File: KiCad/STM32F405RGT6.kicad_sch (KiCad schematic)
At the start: 1 part, among them U1 STM32F405RGTx

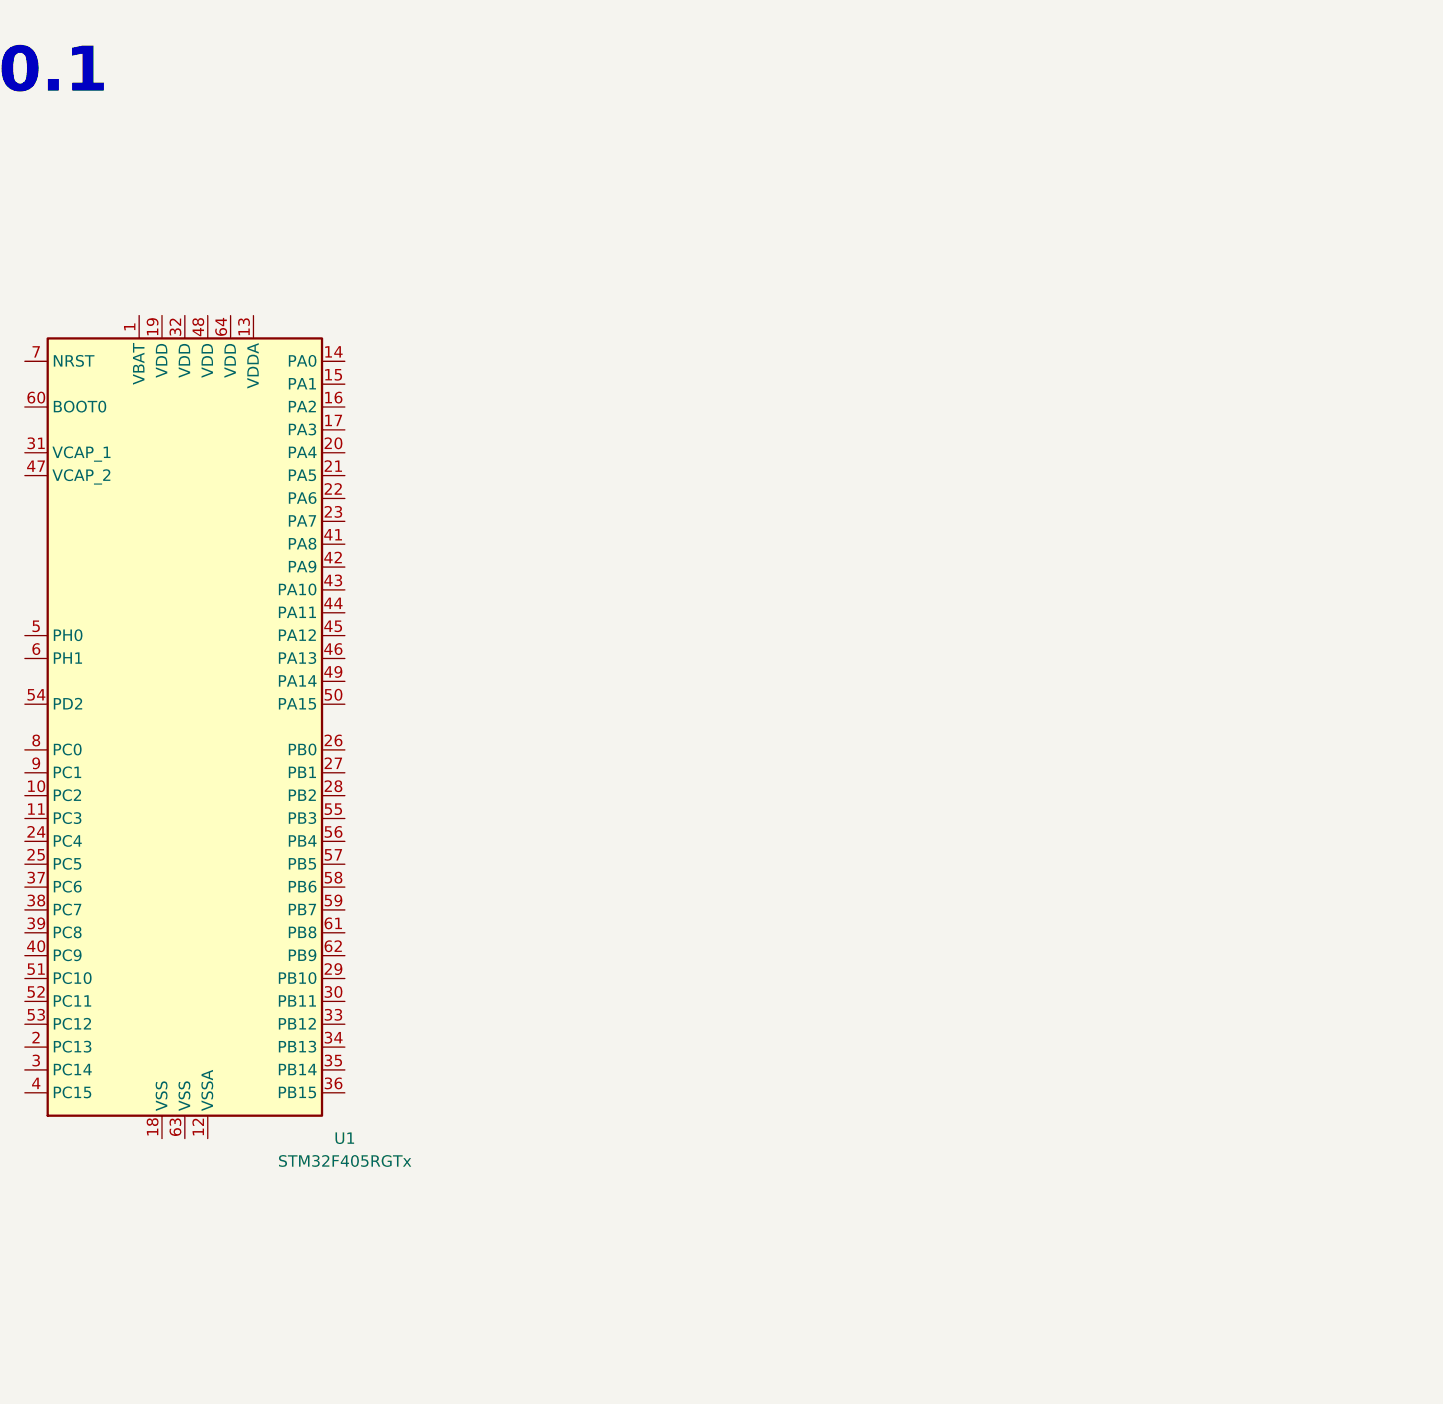
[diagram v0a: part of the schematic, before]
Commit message: Added prototype components to schematic
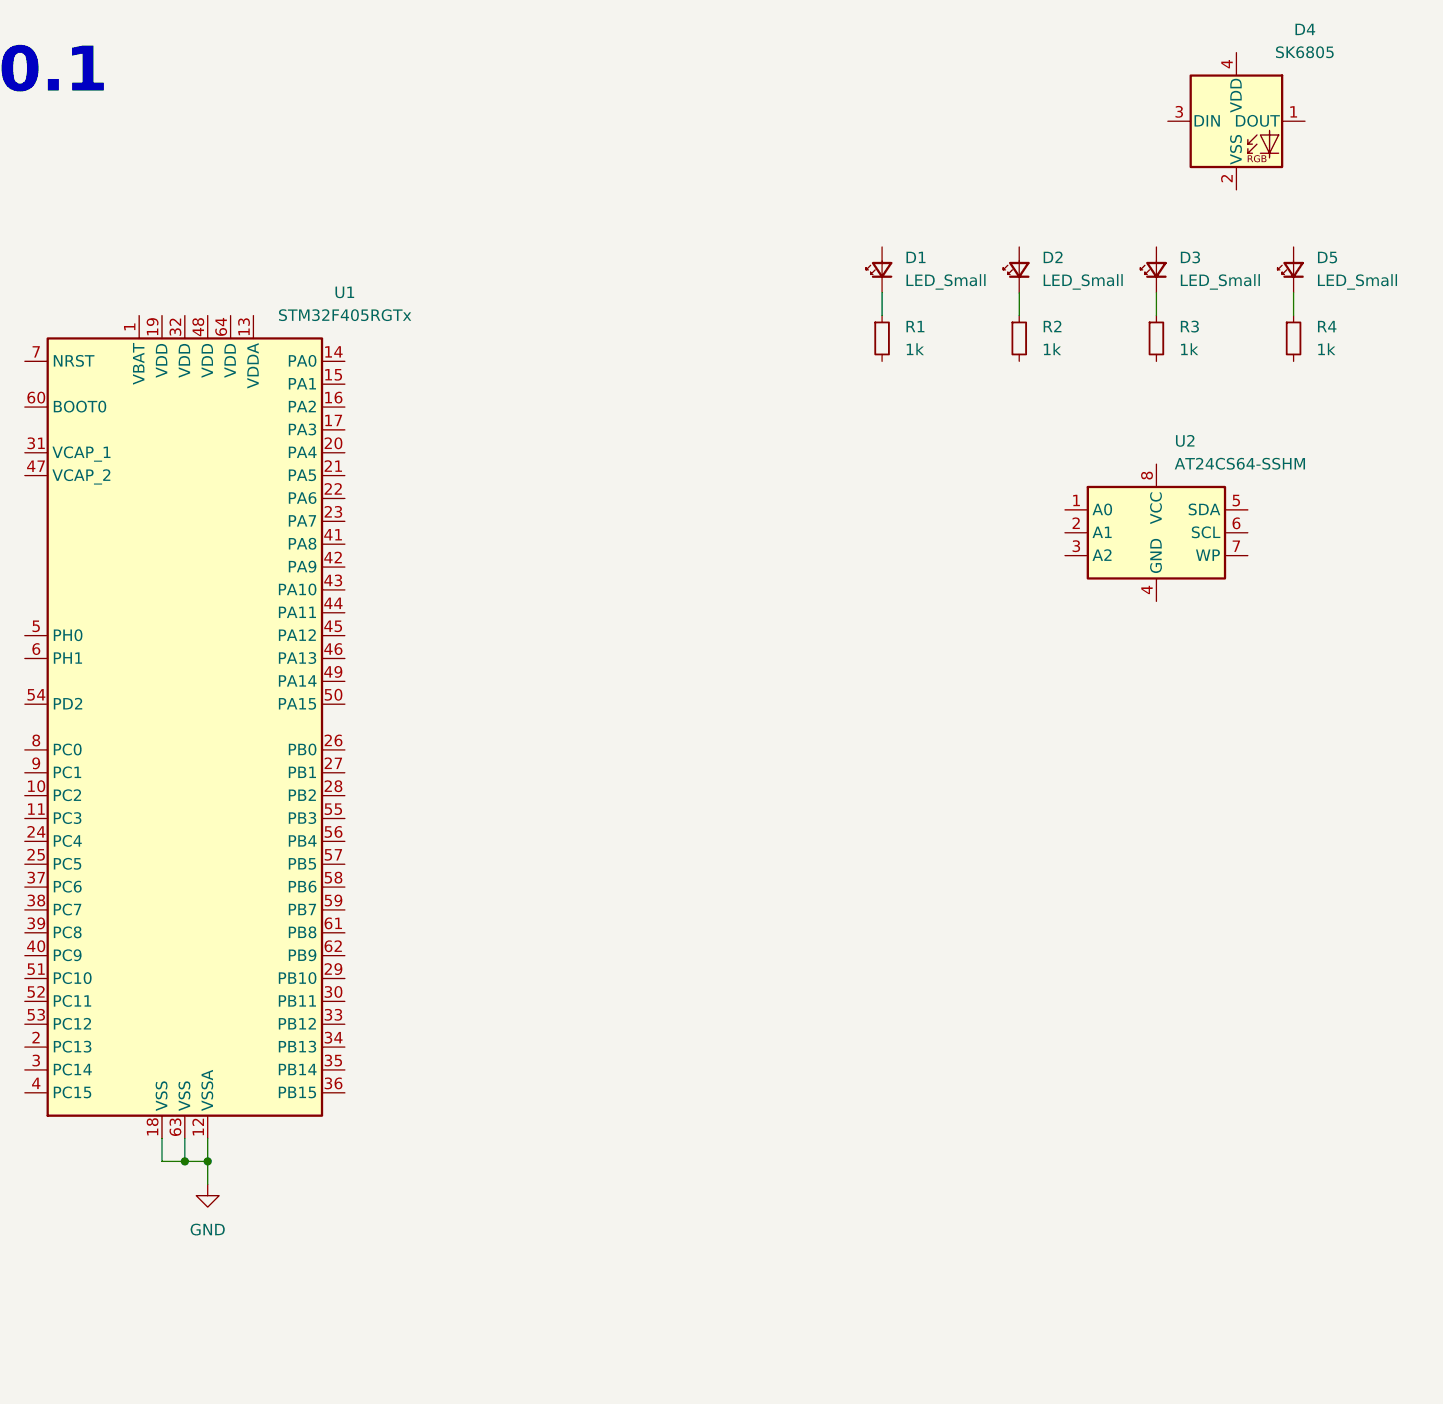
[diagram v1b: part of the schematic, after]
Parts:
- added D1, D2, D3, D5: LED_Small, LED_SMD:LED_0603_1608Metric, symbol Device:LED_Small
- added D4: SK6805, LED_SMD:LED_SK6805_PLCC4_2.4x2.7mm_P1.3mm, symbol LED:SK6805
- added R1, R2, R3, R4: 1k, Resistor_SMD:R_0603_1608Metric, symbol Device:R_Small
- added U2: AT24CS64-SSHM, Package_SO:SOIC-8_3.9x4.9mm_P1.27mm, symbol Memory_EEPROM:AT24CS64-SSHM
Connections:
- net GND: now reaches U1.12 (VSSA)
- net GND: now also U1.18 (VSS), U1.63 (VSS)
- new net: D3.1 (K), R3.1
- new net: D2.1 (K), R2.1
- new net: D1.1 (K), R1.1
- new net: D5.1 (K), R4.1

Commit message: Added Components to the Schematic and PCB
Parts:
- added C1, C11, C3, C5, C7, C8, C9: 100nF, Capacitor_SMD:C_0603_1608Metric, symbol Device:C_Small
- added C10: 1uF, Capacitor_SMD:C_0805_2012Metric, symbol Device:C_Small
- added C2: 10uF, Capacitor_SMD:C_0805_2012Metric, symbol Device:C_Small
- added C4, C6: 2.2uF, Capacitor_SMD:C_0805_2012Metric, symbol Device:C_Small
- added D6, D7: LED_Small, LED_SMD:LED_0603_1608Metric, symbol Device:LED_Small
- added FB1, FB2: FerriteBead_Small, Inductor_SMD:L_0805_2012Metric, symbol Device:FerriteBead_Small
- added J1, J2: USB_C_Receptacle_USB2.0, Connector_USB:USB_C_Receptacle_HRO_TYPE-C-31-M-12, symbol Connector:USB_C_Receptacle_USB2.0
- added R5, R6: 1k, Resistor_SMD:R_0603_1608Metric, symbol Device:R_Small
- added SW1: SW_SPST, symbol Switch:SW_SPST
- added U3: FT232BM, Package_QFP:LQFP-32_7x7mm_P0.8mm, symbol Interface_USB:FT232BM
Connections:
- net GND: now also C1.2, C10.2, C11.2, C2.2, C3.2, C4.2, C5.2, C6.2, C7.2, C8.2, C9.2, SW1.1 (A)
- net VDD_Decoupling: now reaches U1.1 (VBAT)
- net VDD_Decoupling: now also U1.19 (VDD), U1.32 (VDD), U1.48 (VDD), U1.64 (VDD), C11.1, C2.1, C3.1, C5.1, C7.1, C8.1, FB1.2
- net VDDA_Decoupling: now reaches U1.13 (VDDA)
- net VDDA_Decoupling: now also C10.1, C9.1, FB2.1
- net at U1.31 (VCAP_1): now also C4.1
- net STM32_USBD-: now reaches U1.35 (PB14)
- net STM32_USBD-: now also J1.A7 (D-), J1.B7 (D-)
- net STM32_USBD+: now reaches U1.36 (PB15)
- net STM32_USBD+: now also J1.A6 (D+), J1.B6 (D+)
- net FTDI_RX: now reaches U1.42 (PA9)
- net FTDI_RX: now also U3.24 (D1/RXD)
- net FTDI_TX: now reaches U1.43 (PA10)
- net FTDI_TX: now also U3.25 (D0/TXD)
- net at U1.47 (VCAP_2): now also C6.1
- net +3V3: now reaches U1.7 (NRST)
- net +3V3: now also C1.1, D6.2 (A), D7.2 (A), FB1.1, FB2.2, SW1.2 (B), U3.23 (D2/~{RST})
- new net: D6.1 (K), R5.1
- new net: J1.A1 (GND), J1.A12 (GND), J1.B1 (GND), J1.B12 (GND)
- new net: J1.A4 (VBUS), J1.A9 (VBUS), J1.B4 (VBUS), J1.B9 (VBUS)
- new net: D7.1 (K), R6.1
- new net: J2.A1 (GND), J2.A12 (GND), J2.B1 (GND), J2.B12 (GND)
- new net: J2.A4 (VBUS), J2.A9 (VBUS), J2.B4 (VBUS), J2.B9 (VBUS)
- new net FTDI_CTS: U3.22 (D3/~{CTS})
- new net FTDI_DTR: U3.21 (D4/~{DTR})
- new net FTDI_USBD+: J2.A6 (D+), J2.B6 (D+), U3.7 (USBDP)
- new net FTDI_USBD-: J2.A7 (D-), J2.B7 (D-), U3.8 (USBDM)
- new net RX_LED: R5.2, U3.11 (~{RXLED})
- new net TX_LED: R6.2, U3.12 (~{TXLED})
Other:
- moved on the sheet: D1, D2, D3, D4, D5, R1, R2, R3, R4, U1, U2

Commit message: Updated Schematic and PCB
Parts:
- added C12, C13: 14pF, Capacitor_SMD:C_0603_1608Metric, symbol Device:C_Small
- added JP1: BOOT0, Connector_PinHeader_2.54mm:PinHeader_1x02_P2.54mm_Vertical, symbol Jumper:Jumper_2_Open
- added R7, R9: 10k, Resistor_SMD:R_0603_1608Metric, symbol Device:R_Small
- added R8: 470R, Resistor_SMD:R_0603_1608Metric, symbol Device:R_Small
- added Y1: 25MHz, Crystal:Crystal_SMD_3225-4Pin_3.2x2.5mm, symbol Device:Crystal_GND24_Small
- D4: footprint LED_SMD:LED_SK6805_PLCC4_2.4x2.7mm_P1.3mm -> LED_SMD:LED_SK6812_EC15_1.5x1.5mm
- FB1, FB2: value FerriteBead_Small -> 100R @100MHz
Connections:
- net +3V3: now also JP1.2 (B)
- net GND: now also C12.1, C13.2, R7.2, R9.2, Y1.2, Y1.4
- net at U1.28 (PB2): now also R9.1
- net VCAP_1: now reaches C4.1, U1.31 (VCAP_1)
- net VCAP_2: now reaches C6.1, U1.47 (VCAP_2)
- net HSE_IN: now reaches U1.5 (PH0)
- net HSE_IN: now also C12.2, Y1.1
- net HSE_OUT: now reaches U1.6 (PH1)
- net HSE_OUT: now also R8.1
- net BOOT0: now reaches U1.60 (BOOT0)
- net BOOT0: now also JP1.1 (A), R7.1
- new net: C13.1, R8.2, Y1.3
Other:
- moved on the sheet: D1, D2, D3, D5, R1, R2, R3, R4

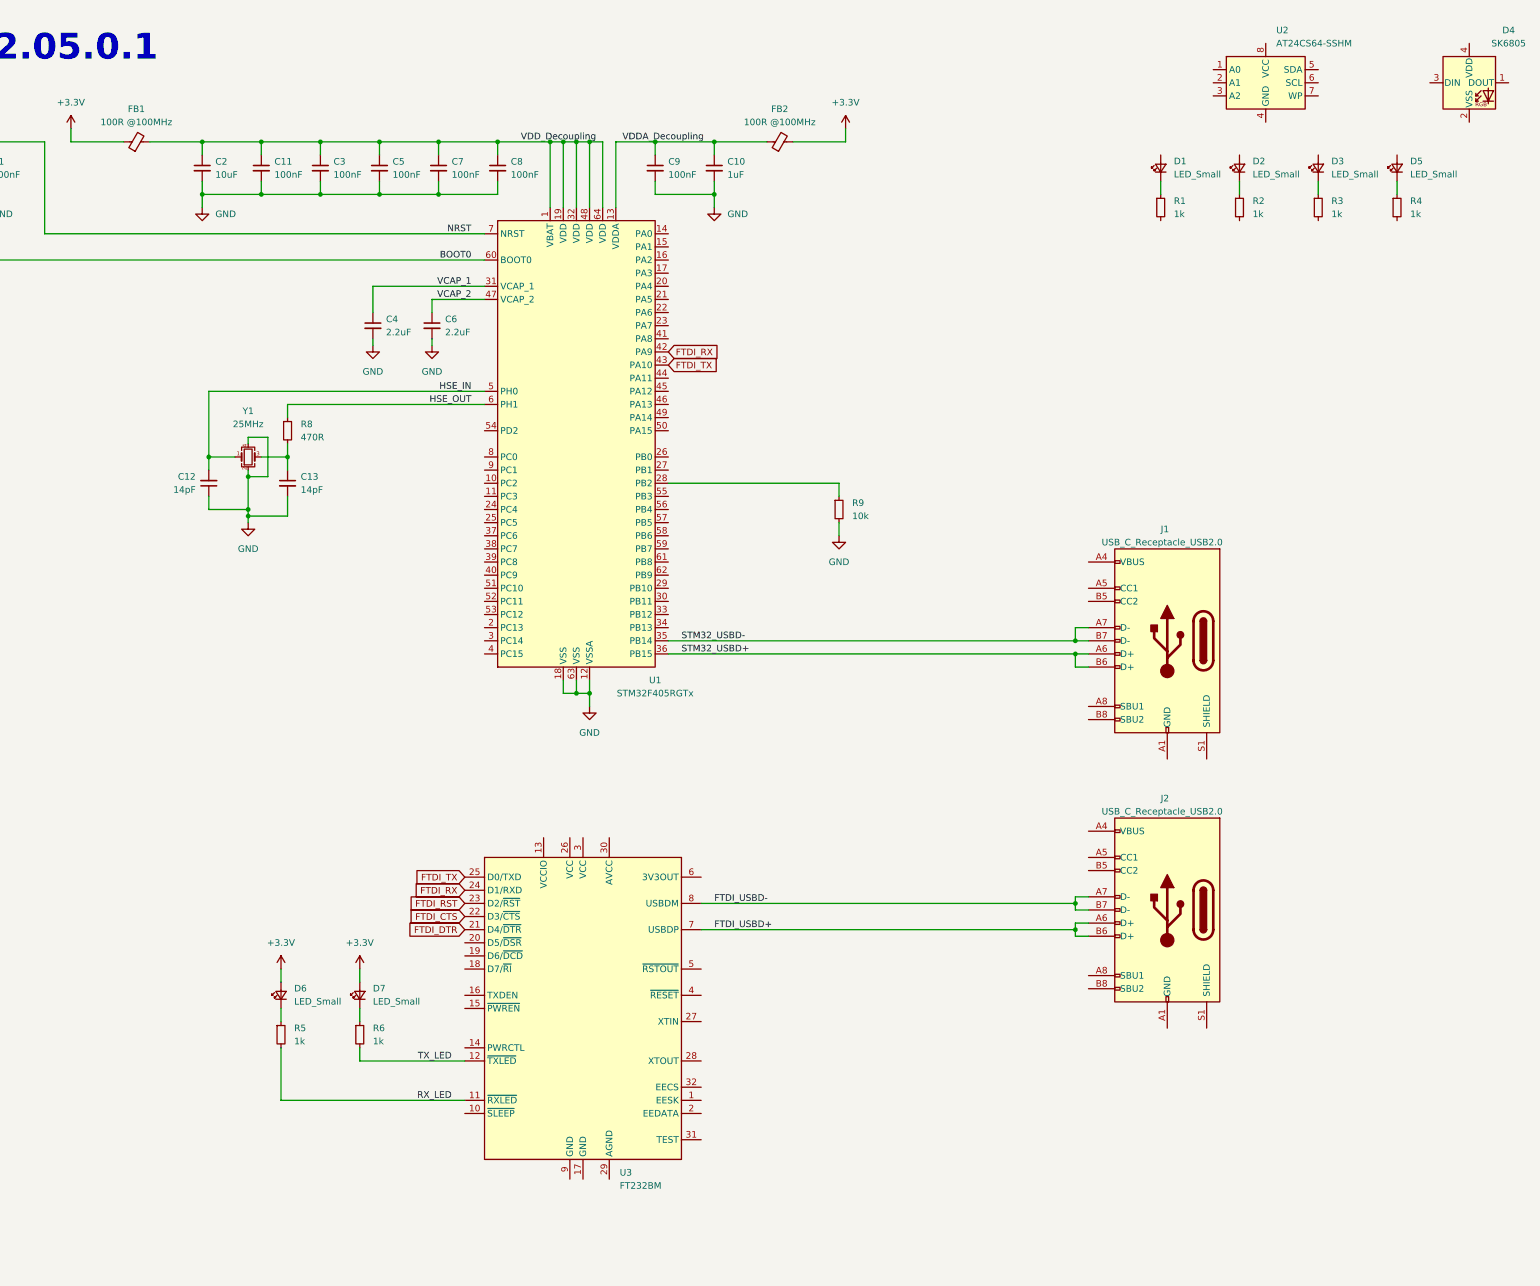
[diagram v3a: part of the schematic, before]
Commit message: Added components to schematic
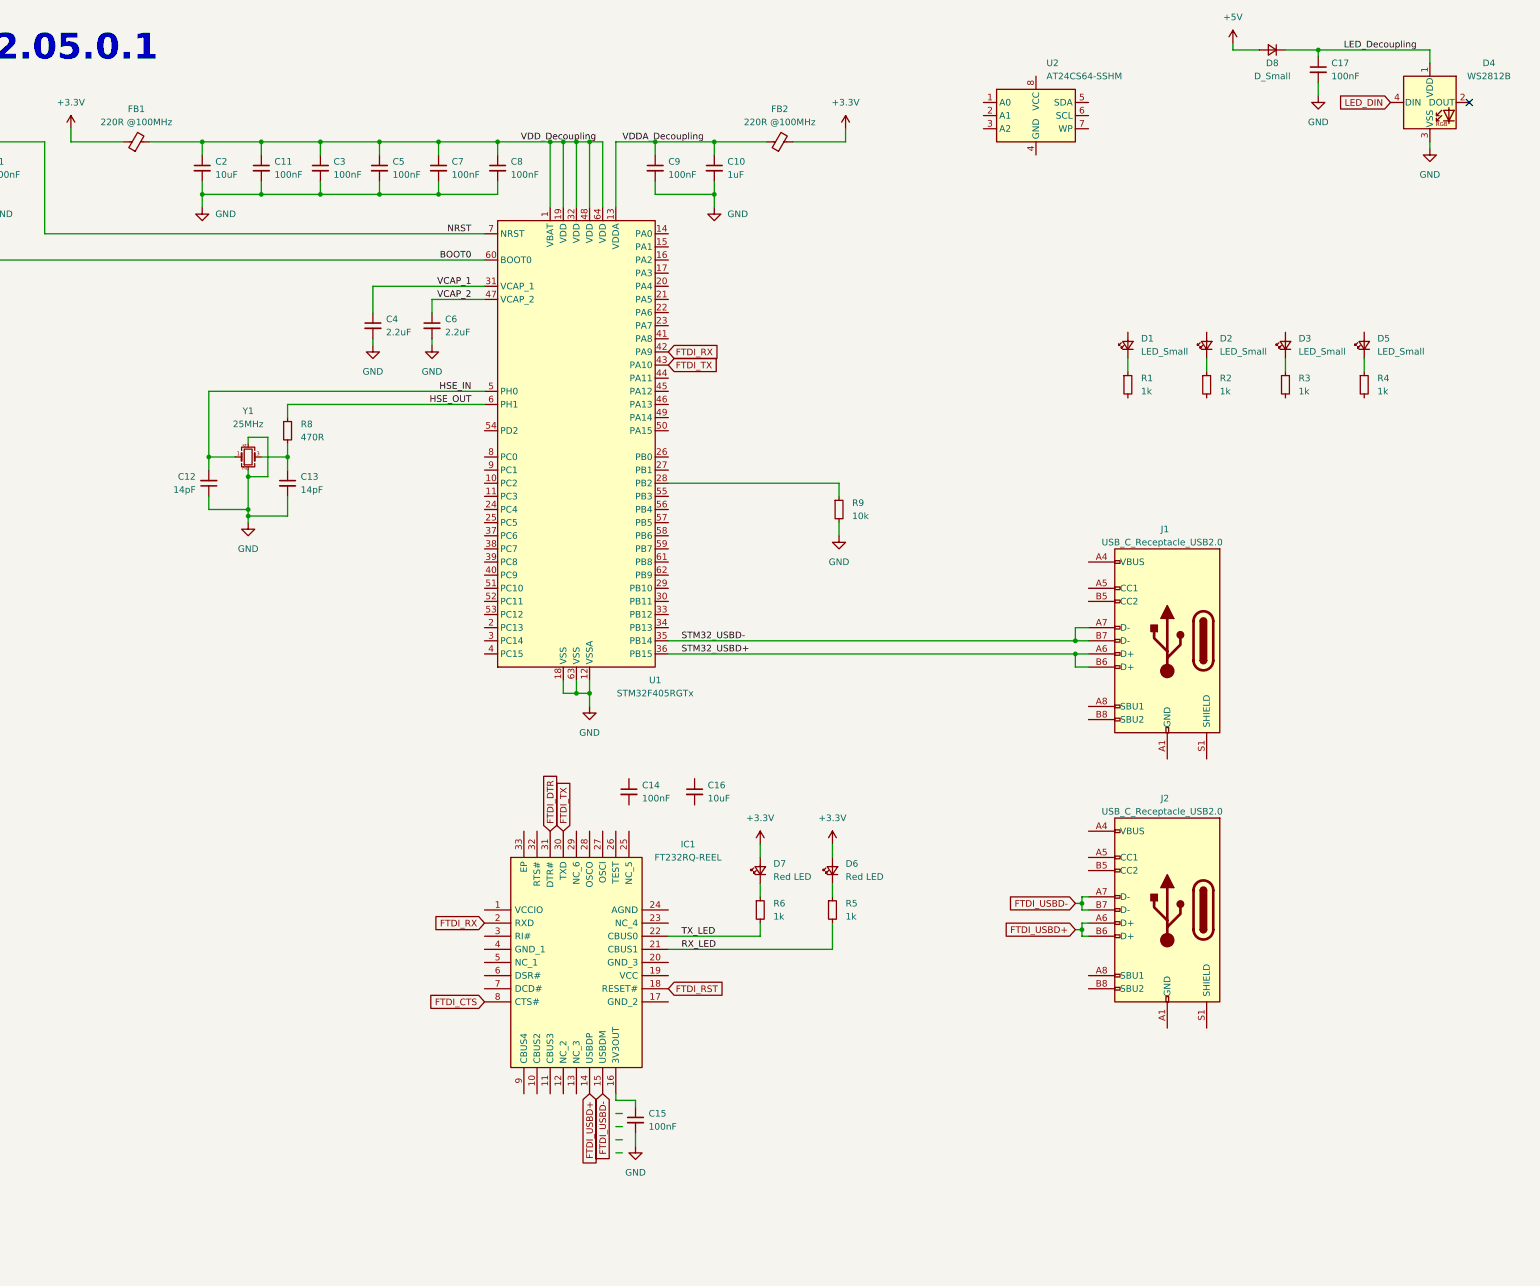
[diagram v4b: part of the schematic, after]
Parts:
- removed D4: SK6805, LED_SMD:LED_SK6812_EC15_1.5x1.5mm, symbol LED:SK6805
- removed U3: FT232BM, Package_QFP:LQFP-32_7x7mm_P0.8mm, symbol Interface_USB:FT232BM
- added C14, C15, C17: 100nF, Capacitor_SMD:C_0603_1608Metric, symbol Device:C_Small
- added C16: 10uF, Capacitor_SMD:C_0603_1608Metric, symbol Device:C_Small
- added D4: WS2812B, LED_SMD:LED_WS2812B_PLCC4_5.0x5.0mm_P3.2mm, symbol LED:WS2812B
- added D8: D_Small, Diode_SMD:D_0603_1608Metric, symbol Device:D_Small
- added IC1: FT232RQ-REEL, Package_DFN_QFN:QFN-32-1EP_5x5mm_P0.5mm_EP3.3x3.3mm_ThermalVias, symbol FT232RQ-REEL:FT232RQ-REEL
- C10, C2, C4, C6: footprint Capacitor_SMD:C_0805_2012Metric -> Capacitor_SMD:C_0603_1608Metric
- D6, D7: value LED_Small -> Red LED
- FB1, FB2: value 100R @100MHz -> 220R @100MHz; footprint Inductor_SMD:L_0805_2012Metric -> Inductor_SMD:L_0603_1608Metric; Mouser Part Number (none) -> 810-MMZ1608Y221BTA00; Part Number (none) -> MMZ1608Y221BTA00
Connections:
- net +3V3: now also IC1.18 (RESET#)
- net FTDI_CTS: now also IC1.8 (CTS#)
- net FTDI_DTR: now also IC1.31 (DTR#)
- net FTDI_RX: now also IC1.2 (RXD)
- net FTDI_TX: now also IC1.30 (TXD)
- net FTDI_USBD+: now also IC1.14 (USBDP)
- net FTDI_USBD-: now also IC1.15 (USBDM)
- net GND: now also C15.2, C17.2, D4.3 (VSS)
- net RX_LED: now also IC1.21 (CBUS1)
- net TX_LED: now also IC1.22 (CBUS0)
- new net: C15.1, IC1.16 (3V3OUT)
- new net +5V: D8.2 (A)
- new net LED_DIN: D4.4 (DIN)
- new net LED_Decoupling: C17.1, D4.1 (VDD), D8.1 (K)
- no-connect marks 0 -> 1
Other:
- moved on the sheet: D1, D2, D3, D5, D6, D7, R1, R2, R3, R4, R5, R6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
